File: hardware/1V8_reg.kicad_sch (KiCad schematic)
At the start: 4 parts, among them U7 AP2127K-1.8

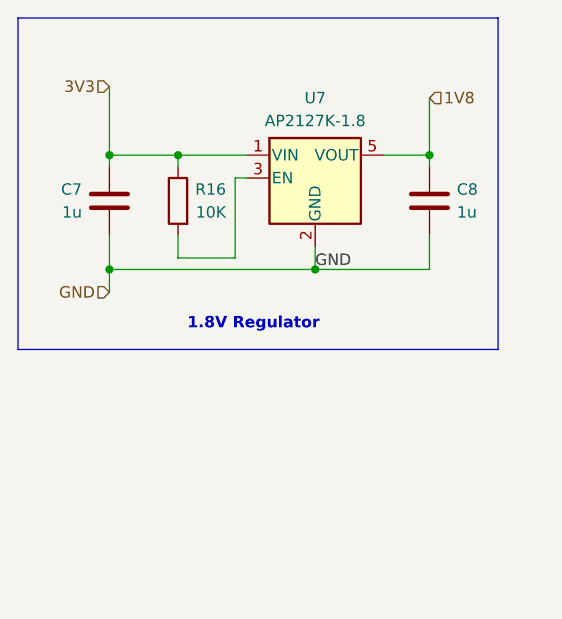
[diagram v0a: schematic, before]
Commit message: organized schem and updated readme
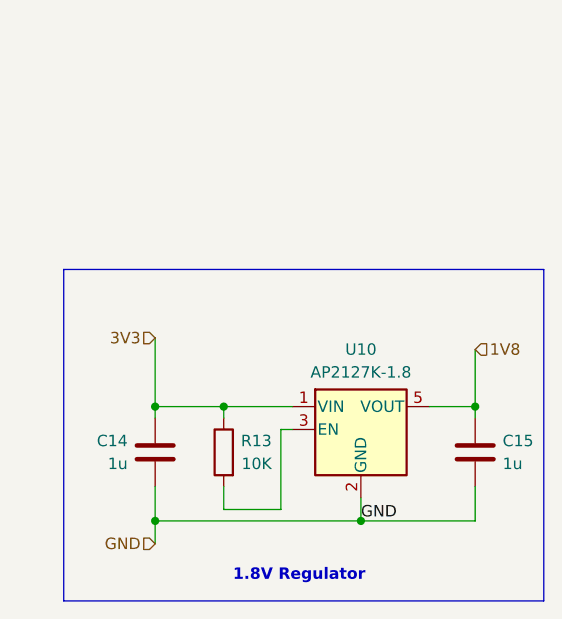
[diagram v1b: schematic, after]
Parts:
- renumbered C7 to C14, C8 to C15, R16 to R13, U7 to U10
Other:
- moved on the sheet: C14, C15, R13, U10

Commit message: completed board
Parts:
- C14, C15: footprint (none) -> Capacitor_SMD:C_1206_3216Metric_Pad1.33x1.80mm_HandSolder
- R16: renamed from R13; footprint (none) -> Resistor_SMD:R_1206_3216Metric_Pad1.30x1.75mm_HandSolder
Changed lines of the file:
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@@
 		(on_board yes)
 		(dnp no)
-		(property "Reference" "R13"
+		(property "Reference" "R16"
 			(at 141.224 97.79 0)
 			(effects
@@
 			)
 		)
-		(property "Footprint" ""
+		(property "Footprint" "Resistor_SMD:R_1206_3216Metric_Pad1.30x1.75mm_HandSolder"
 			(at 137.668 99.06 90)
 			(effects
@@
 			(project "BREAD_Slice"
 				(path "/66043bca-a260-4915-9fce-8a51d324c687/2f5b6331-fe72-4ecd-809e-6c5537e7b8a8"
-					(reference "R13")
+					(reference "R16")
 					(unit 1)
 				)
@@
 			)
 		)
-		(property "Footprint" ""
+		(property "Footprint" "Capacitor_SMD:C_1206_3216Metric_Pad1.33x1.80mm_HandSolder"
 			(at 127.3048 102.87 0)
 			(effects
@@
 			)
 		)
-		(property "Footprint" ""
+		(property "Footprint" "Capacitor_SMD:C_1206_3216Metric_Pad1.33x1.80mm_HandSolder"
 			(at 164.7952 102.87 0)
 			(effects

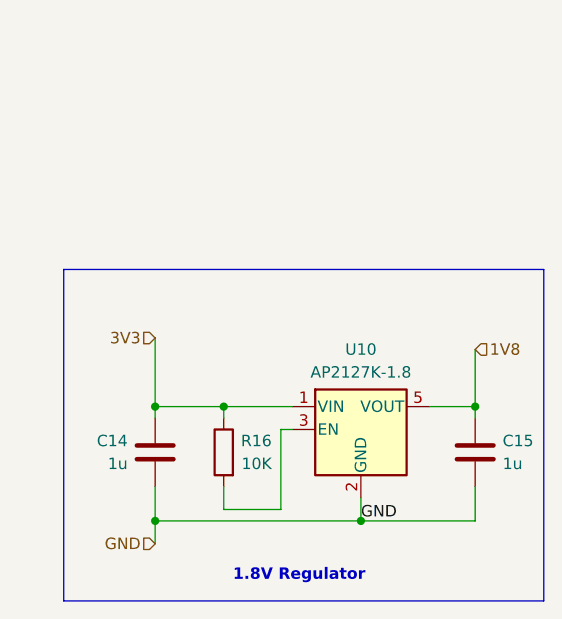
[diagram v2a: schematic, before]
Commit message: final touches for order and assembly
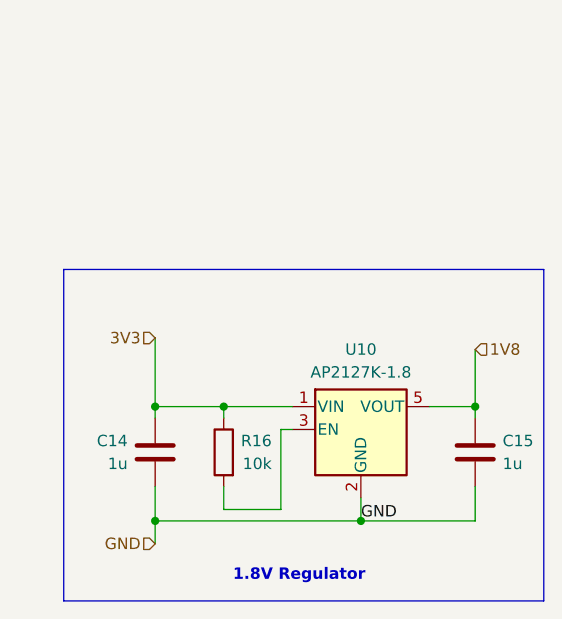
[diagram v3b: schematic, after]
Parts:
- R16: value 10K -> 10k
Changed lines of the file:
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@@
 			)
 		)
-		(property "Value" "10K"
+		(property "Value" "10k"
 			(at 141.224 100.33 0)
 			(effects
